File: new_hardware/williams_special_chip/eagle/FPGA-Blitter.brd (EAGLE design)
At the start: 68.6 x 68.6 mm, 3 parts

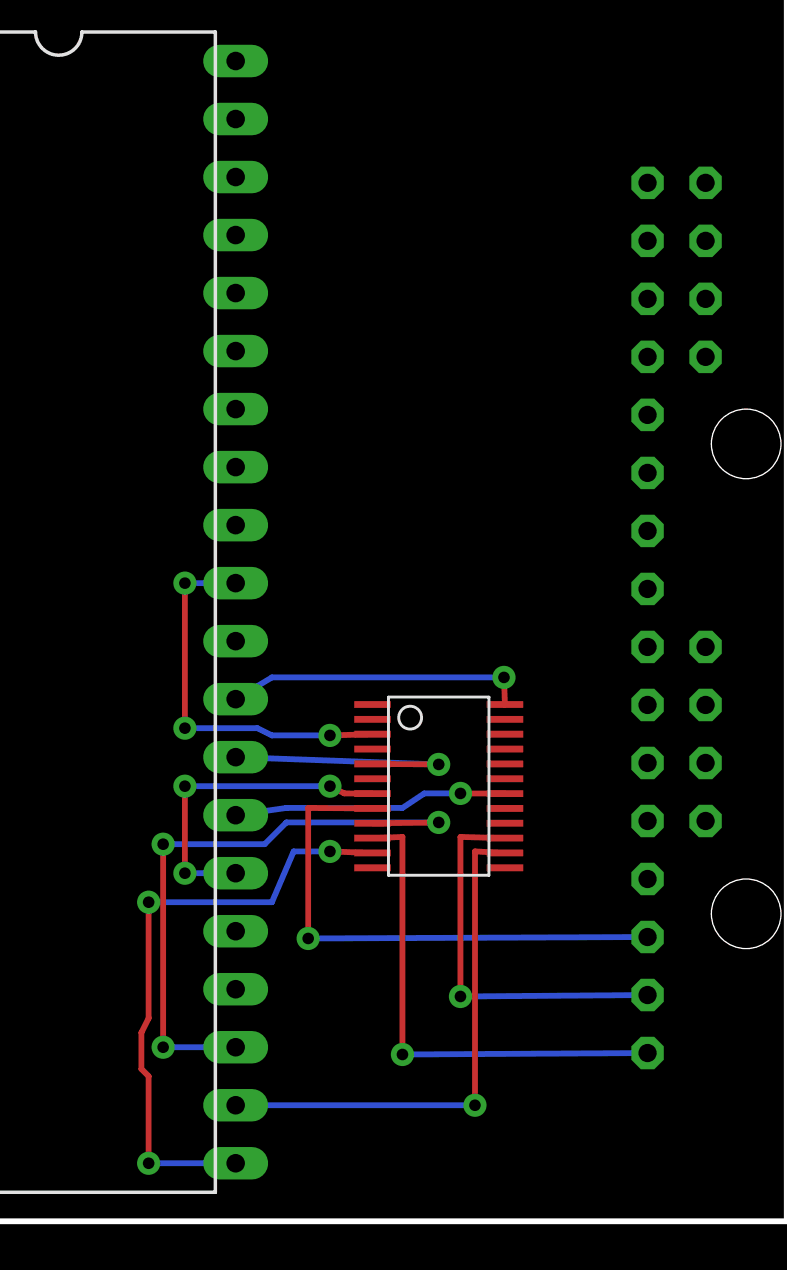
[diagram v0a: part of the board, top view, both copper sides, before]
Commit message: added 20 I/O line quickswitch part.  about to try auto-router
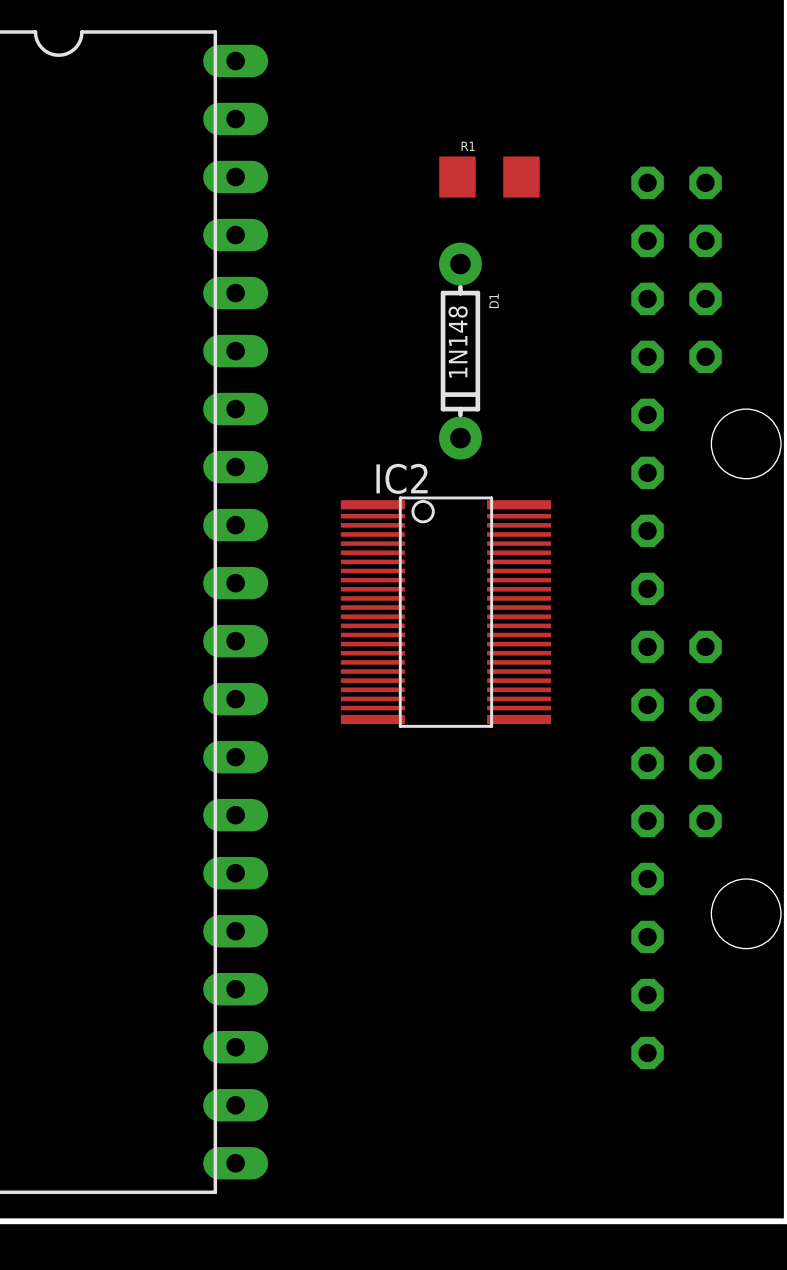
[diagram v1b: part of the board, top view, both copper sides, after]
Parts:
- removed U$1: SN74CBTD3384, mpo:TSSOP24
- added D1: 1N148, SparkFun:DIODE-1N4148
- added IC2: IDTQS32X861, mpo:QVSOP-DJG48-IDT
- added R1: 10k, SparkFun:1206
- IC1: value (none) -> SPECIAL_CHIP
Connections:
- removed net A10_3V3: U$1.23
- new net N$8: D1.C, IC2.36, IC2.48, R1.1
- net !CS: now also IC2.19; no longer U$1.16
- net !CS_3V3: now also IC2.29; no longer U$1.17
- net !RESET: now also IC2.7
- net !WINH: now also IC2.3
- net 4MHZ: now also IC2.8
- net A0: now also IC2.16; no longer U$1.5
- net A0_3V3: now also IC2.32; no longer U$1.4
- net A1: now also IC2.17; no longer U$1.18
- net A10: now also IC2.11; no longer U$1.22
- net A11: now also IC2.10
- net A12: now also IC2.9
- net A13: now also IC2.6
- net A14: now also IC2.5
- net A15: now also IC2.4
- net A1_3V3: now also IC2.31; no longer U$1.19
- net A2: now also IC2.18; no longer U$1.7
- net A2_3V3: now also IC2.30; no longer U$1.6
- net A5: now also IC2.23; no longer U$1.11
- net A5_3V3: now also IC2.25; no longer U$1.10
- net A6: now also IC2.22; no longer U$1.14
- net A6_3V3: now also IC2.26; no longer U$1.15
- net A7: now also IC2.21; no longer U$1.9
- net A7_3V3: now also IC2.27; no longer U$1.8
- net A8: now also IC2.15; no longer U$1.20
- net A8_3V3: now also IC2.33; no longer U$1.21
- net A9: now also IC2.14; no longer U$1.3
- net A9_3V3: now also IC2.34; no longer U$1.2
- net GND: now also IC2.12, IC2.24, IC2.35, IC2.47, R1.2; no longer U$1.1, U$1.12, U$1.13
- net VCC: now also D1.A; no longer U$1.24
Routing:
- net A7: track 27.4 -> 0.00 mm, vias 3 -> 0
- net A5: track 26.7 -> 0.00 mm, vias 3 -> 0
- net A7_3V3: track 23.4 -> 0.00 mm, vias 1 -> 0
- net A6: track 22.9 -> 0.00 mm, vias 1 -> 0
- net A5_3V3: track 21.6 -> 0.00 mm, vias 1 -> 0
- net A6_3V3: track 17.1 -> 0.00 mm, vias 1 -> 0
- net A9: track 16.9 -> 0.00 mm, vias 3 -> 0
- net A2: track 14.3 -> 0.00 mm, vias 3 -> 0
- net VCC: track 13.2 -> 0.00 mm, vias 1 -> 0
- net A1: track 12.0 -> 0.00 mm, vias 1 -> 0
- net A0: track 11.8 -> 0.00 mm, vias 1 -> 0

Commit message: got one half finished
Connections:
- new net A10_3V3: IC2.37, U$2.C7
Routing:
- net VCC: track 0.00 -> 98.1 mm
- net N$8: track 0.00 -> 29.4 mm
- net A5: track 0.00 -> 29.1 mm, vias 0 -> 1
- net !WINH: track 0.00 -> 28.3 mm, vias 0 -> 1
- net A6: track 0.00 -> 28.3 mm, vias 0 -> 1
- net A15: track 0.00 -> 27.9 mm, vias 0 -> 1
- net A7: track 0.00 -> 27.7 mm, vias 0 -> 1
- net A14: track 0.00 -> 26.4 mm, vias 0 -> 1
- net !CS: track 0.00 -> 24.5 mm, vias 0 -> 1
- net A6_3V3: track 0.00 -> 22.5 mm, vias 0 -> 1
- net A7_3V3: track 0.00 -> 20.8 mm, vias 0 -> 1
- net A13: track 0.00 -> 20.0 mm, vias 0 -> 1
- net A5_3V3: track 0.00 -> 19.8 mm
- net !CS_3V3: track 0.00 -> 19.2 mm, vias 0 -> 1
- net A2_3V3: track 0.00 -> 18.6 mm, vias 0 -> 1
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
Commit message: gotta just verify pins chosen and this is ready for production
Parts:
- added D2: 1N148, SparkFun:DIODE-1N4148
- added IC3, IC4: IDTQS3861, mpo:TSSOP24
- added R2: 10k, SparkFun:1206
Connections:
- removed net N$1: U$2.AL_5V
- removed net N$2: U$2.AU_5V
- removed net N$3: U$2.BL_5V
- new net !BA-BS_3V3: IC3.8, U$2.B4
- new net !HALT_3V3: IC3.7, U$2.B3
- new net !HTCF_3V3: IC3.5, U$2.B1
- new net !RESET_3V3: IC2.41, U$2.C3
- new net !TCF_3V3: IC3.4, U$2.B0
- new net !WINH_3V3: IC2.45, U$2.A15
- new net 4MHZ_3V3: IC2.40, U$2.C4
- new net A11_3V3: IC2.38, U$2.C6
- new net A12_3V3: IC2.39, U$2.C5
- new net A13_3V3: IC2.42, U$2.C2
- new net A14_3V3: IC2.43, U$2.C1
- new net A15_3V3: IC2.44, U$2.C0
- new net A3_3V3: IC4.10, U$2.B14
- new net A4_3V3: IC4.11, U$2.B15
- new net D0_3V3: IC4.8, U$2.B12
- new net D1_3V3: IC4.4, U$2.B10
- new net D2_3V3: IC4.3, U$2.B9
- new net D3_3V3: IC4.2, U$2.B8
- new net D4_3V3: IC3.11, U$2.B7
- new net D5_3V3: IC3.10, U$2.B6
- new net D6_3V3: IC3.9, U$2.B5
- new net D7_3V3: IC3.6, U$2.B2
- new net E_3V3: IC3.3, U$2.A14
- new net N$4: D2.C, IC3.24, IC4.24, R2.1
- new net R/!W_3V3: IC4.9, U$2.B13
- new net U/!L_3V3: IC4.5, U$2.B11
- net !BA-BS: now also IC3.16
- net !E: now also IC3.21
- net !HALT: now also IC3.17
- net !HTCF: now also IC3.19
- net !TCF: now also IC3.20
- net A3: now also IC4.14
- net A4: now also IC4.13
- net D0: now also IC4.16
- net D1: now also IC4.20
- net D2: now also IC4.21
- net D3: now also IC4.22
- net D4: now also IC3.13
- net D5: now also IC3.14
- net D6: now also IC3.15
- net D7: now also IC3.18
- net GND: now also IC3.12, IC3.23, IC4.12, IC4.23, R2.2
- net R/!W: now also IC4.15
- net U/!L: now also IC4.19
- net VCC: now also D2.A
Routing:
- net !WINH_3V3: track 0.00 -> 81.1 mm, vias 0 -> 2
- net N$4: track 0.00 -> 40.2 mm
- net A15_3V3: track 0.00 -> 19.6 mm
- net !RESET_3V3: track 0.00 -> 19.5 mm, vias 0 -> 1
- net VCC: track 98.1 -> 116.8 mm
- net A14_3V3: track 0.00 -> 17.7 mm
- net D3_3V3: track 0.00 -> 16.1 mm
- net A13_3V3: track 0.00 -> 15.9 mm
- net D3: track 0.00 -> 15.7 mm
- net D1: track 0.00 -> 15.7 mm, vias 0 -> 2
- net D2_3V3: track 0.00 -> 14.2 mm
- net U/!L: track 0.00 -> 13.9 mm, vias 0 -> 2
- net !E: track 0.00 -> 13.7 mm
- net D1_3V3: track 0.00 -> 13.2 mm
- net D2: track 0.00 -> 13.2 mm
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- added copper zone on layer 1, net GND
- added copper zone on layer 16, net GND
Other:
- board size 68.6 x 68.6 mm -> 68.6 x 54 mm

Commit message: tweaks
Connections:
- removed net E_3V3: IC3.3, U$2.A14
- removed net N$5: U$2.CL_5V
- new net !E_3V3: IC3.3, U$2.A13
- net !RESET_3V3: now also U$2.C2; no longer U$2.C3
- net !WINH_3V3: now also U$2.A14; no longer U$2.A15
- net 4MHZ_3V3: now also U$2.C3; no longer U$2.C4
- net A10_3V3: now also U$2.C6; no longer U$2.C7
- net A11_3V3: now also U$2.C5; no longer U$2.C6
- net A12_3V3: now also U$2.C4; no longer U$2.C5
- net A13_3V3: now also U$2.C1; no longer U$2.C2
- net A14_3V3: now also U$2.C0; no longer U$2.C1
- net A15_3V3: now also U$2.A15; no longer U$2.C0
- net A9_3V3: now also U$2.C7
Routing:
- net A15_3V3: track 19.6 -> 70.1 mm, vias 0 -> 1
- net !E_3V3: track 0.00 -> 12.8 mm, vias 0 -> 1
- net E_3V3: track 12.7 -> 0.00 mm, vias 1 -> 0
- net !WINH_3V3: track 81.1 -> 68.9 mm, vias 2 -> 1
- net A9_3V3: track 0.00 -> 6.46 mm
- net A11_3V3: track 13.0 -> 15.5 mm
- net A14_3V3: track 17.7 -> 20.1 mm
- net !RESET_3V3: track 19.5 -> 21.8 mm
- net A13_3V3: track 15.9 -> 18.2 mm
- net 4MHZ_3V3: track 11.9 -> 14.0 mm
- net A12_3V3: track 9.95 -> 12.1 mm
- net A10_3V3: track 5.96 -> 7.97 mm
- net D3_3V3: track 16.1 -> 15.4 mm

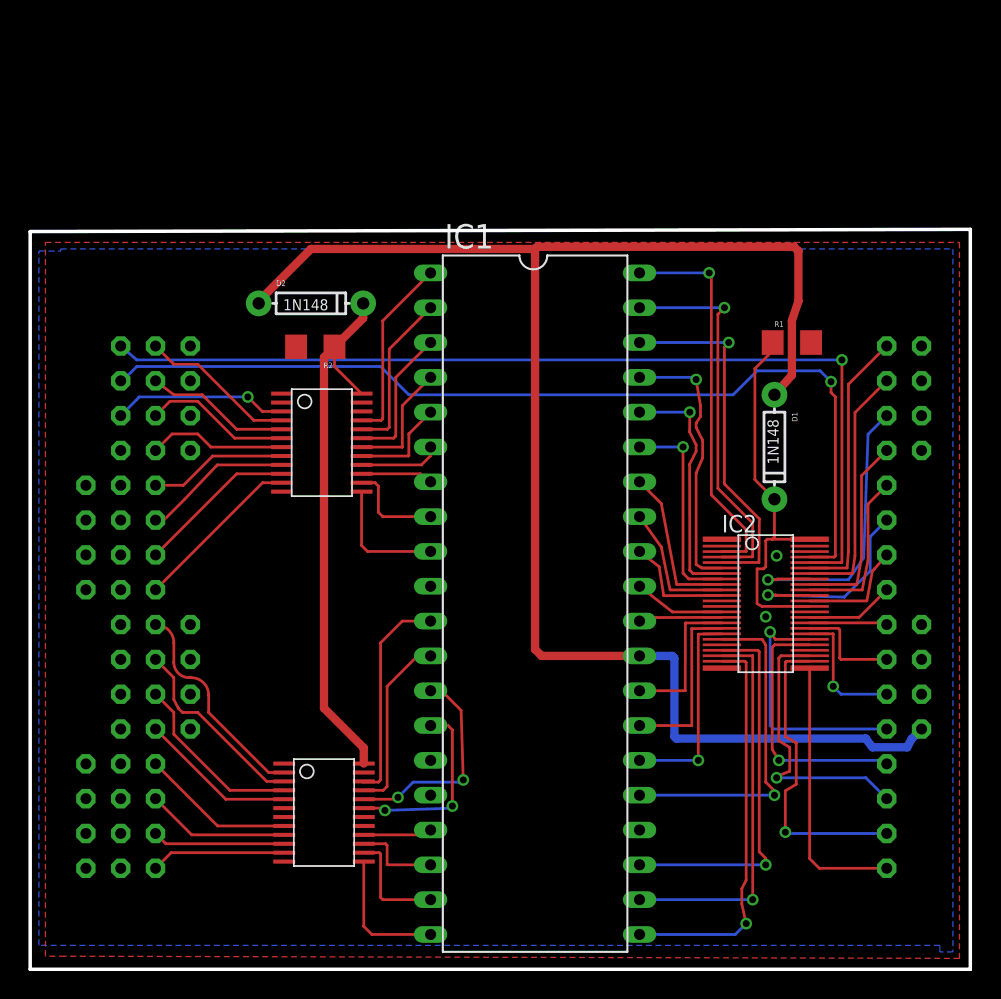
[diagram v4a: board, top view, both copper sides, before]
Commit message: a few touch-ups to board layout
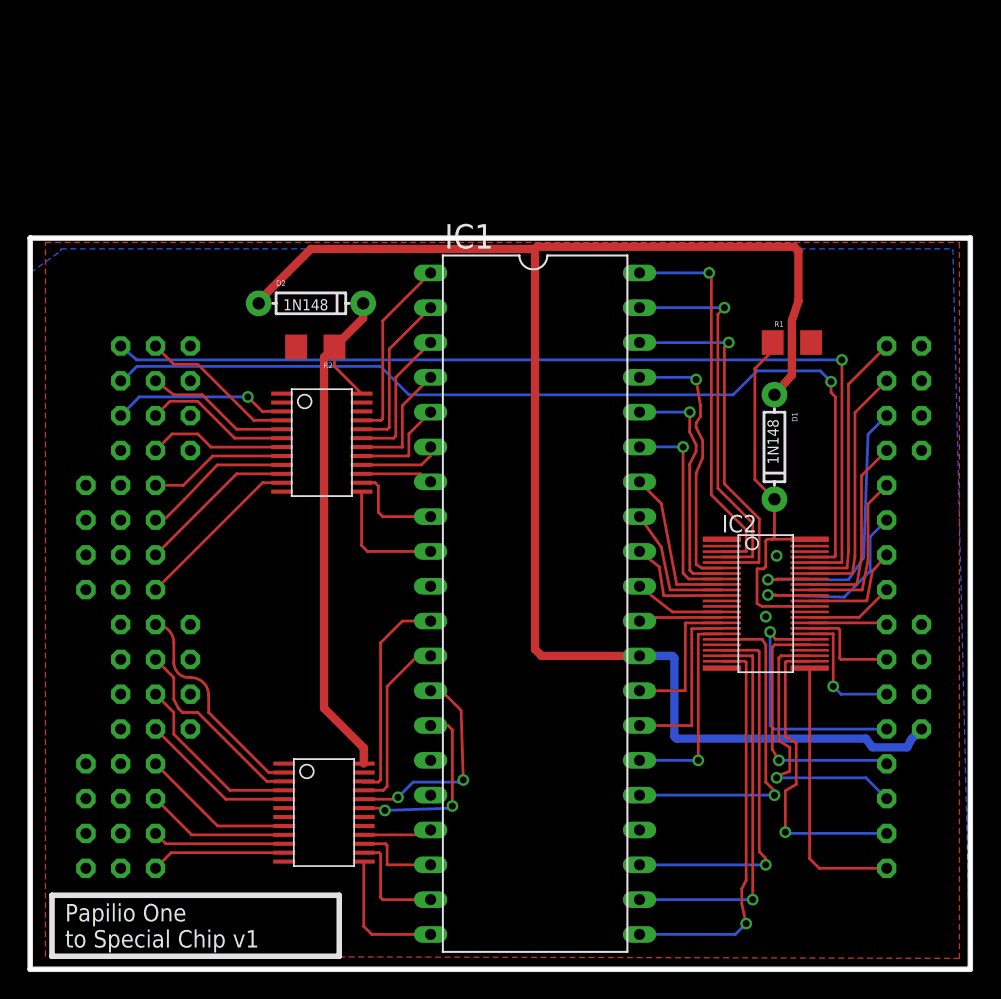
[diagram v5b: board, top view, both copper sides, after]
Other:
- board size 68.6 x 54 mm -> 68.6 x 53.3 mm
- board text added: "Papilio One to Special Chip v1"
